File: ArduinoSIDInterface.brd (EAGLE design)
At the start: 87.3 x 62.2 mm, 26 parts, among them IC1 74HC595N, IC2 74HC595N, IC3 LM7809, IC4 LM7805, T1 BC547

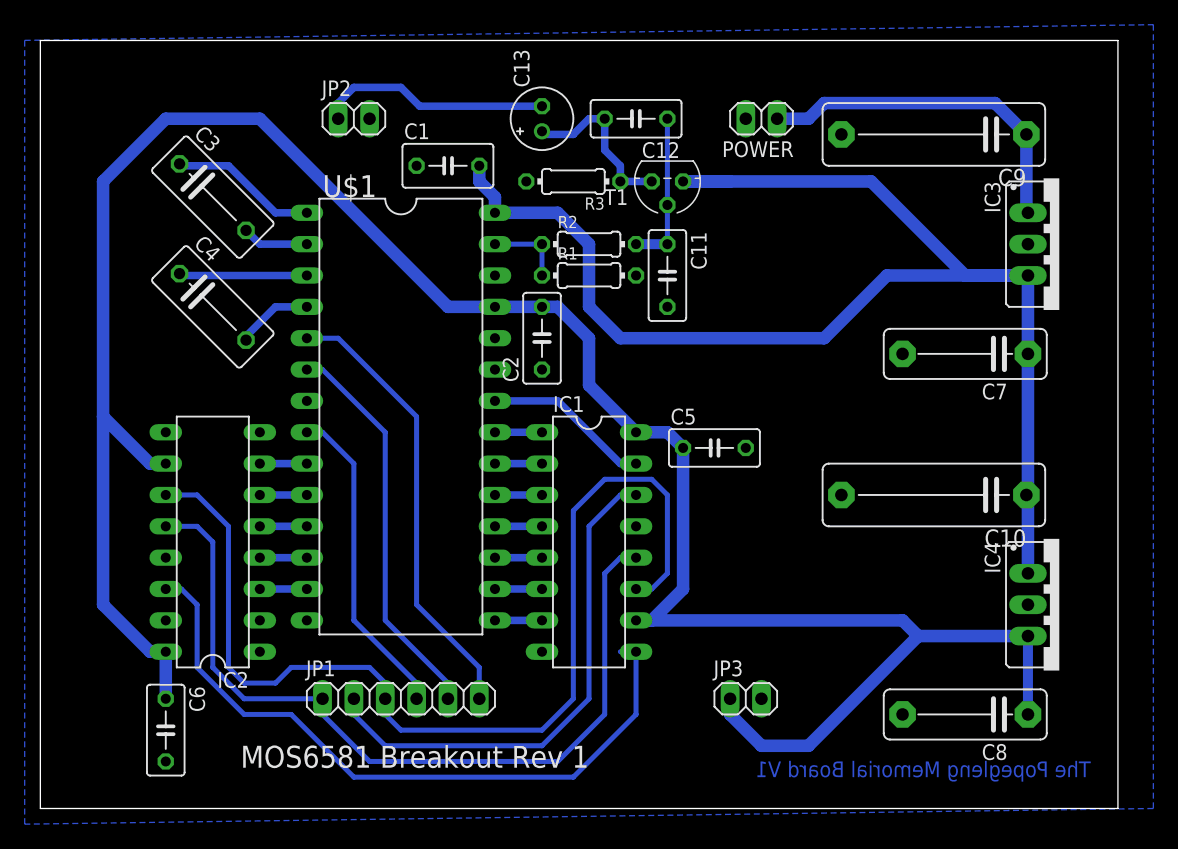
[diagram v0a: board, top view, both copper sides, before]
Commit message: Fixed up trace thickness, ground plane distance etc
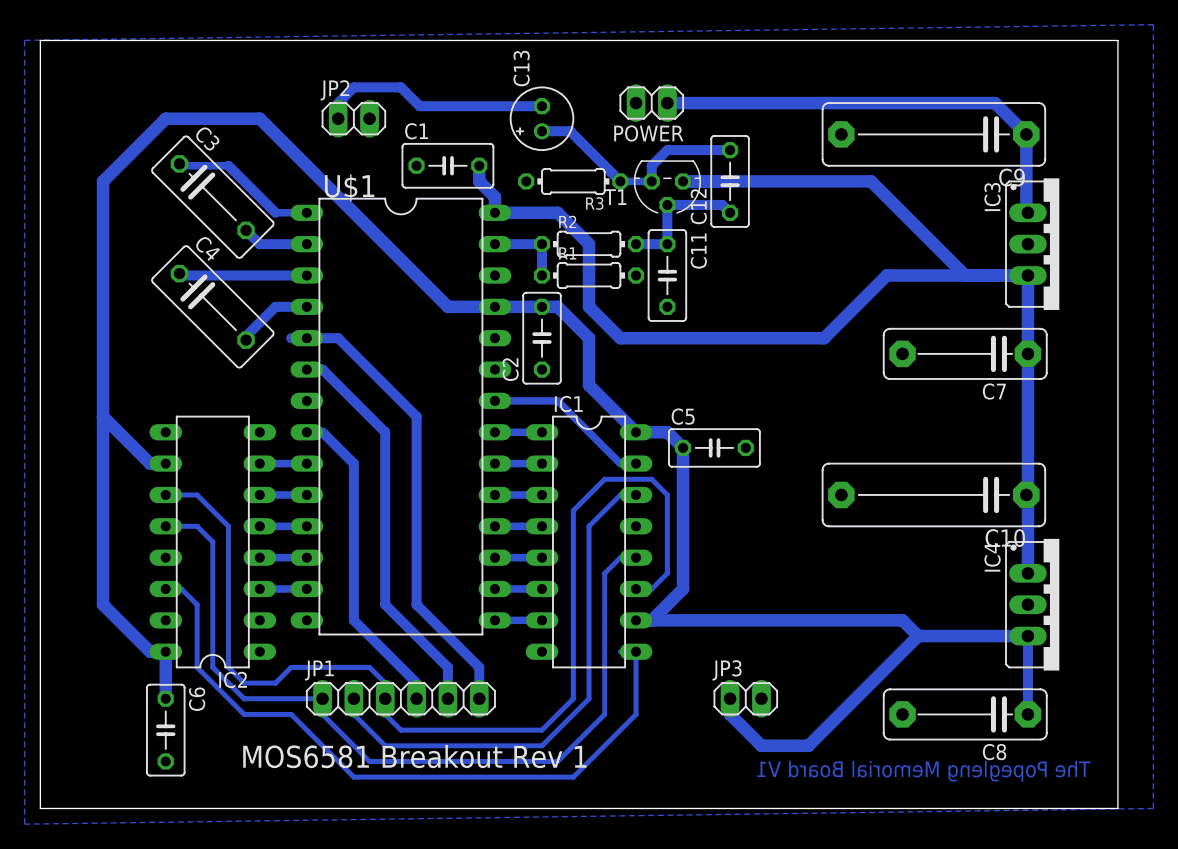
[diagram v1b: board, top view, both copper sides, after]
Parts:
- moved C12 9.16 mm to (55.9, 50.8), turned to 90 degrees
- moved POWER 8.98 mm to (49.5, 57.1)
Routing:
- net V+: track 28.2 -> 36.5 mm
- net N$24: track 13.9 -> 18.7 mm
- net N$22: track 12.7 -> 11.1 mm
- net N$12: track 36.5 -> 37.8 mm
